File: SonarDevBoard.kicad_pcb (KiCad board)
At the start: 6 copper layers, 540 x 106.9 mm, 374 parts, among them J1001 TX_OUT_GAIN, J101 POWER, J102 DEBUG, J103 PORT1, J104 FPGA, J105 ETHERNET, J106 SYNC, J107 SONAR+, J108 SONAR+, J109 SONAR-, J110 SONAR-, J111 TRANSDUCER, J112 MOTOR, J1201 RFBT, J1202 RDAC, J401 RX_IN, J402 PREAMP, J403 BIAS_RES, J404 BIAS_RES, J405 GAIN_RES, J406 LPF_CAP, J407 VARAMP_OUT, J501 LABEL, J502 LABEL, J601 CAP, J901 OCTOSPI, Q101 DMP6023LSS-13, Q1201 SQJ974EP, Q1501 MMBT3904L, Q1502 MMBT3904L, Q1503 MMBT3904L, T101 B65655B0010X000, T701 HR641680E, U1001 SL9062D, U1002 LT1794, U1003 CSA230PASOT235, U101 LIS2DH12TR, U1101 TLV62569DBVR, U1201 LM5122MHX/NOPB, U1202 DAC53401DSGR, U1301 LM27313XMFX/NOPB, U1401 MG78L05T3, U1501 EPC23104ENGRT, U1502 EPC23104ENGRT, U1601 DRV8426RGER, U301 STM32H563AII3Q, U401 MD0100DK6-G, U402 OPA1612AIDR, U403 AD8338ACPZ-R7, U404 WS72552M-8/TR, U601 DAC53401DSGR, U602 DAC53401DSGR, U603 74LVC1G66GW,125, U701 DP83825IRMQR, U801 MIC28517T-E/PHA, U901 S27KL0642DPBHB023, X301 25MHz 8pF

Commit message: Finish VCC boost layout, realize that not enough power can be delivered to it
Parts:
- moved C1210 80.7 mm to (159.3, -76.1), turned to 90 degrees
- moved C1209 79.1 mm to (160.5, -76.1), turned to -90 degrees
- moved C1202 42.3 mm to (182.6, -84.5), turned to 180 degrees
- moved J1201 38.8 mm to (170.2, -89.0), turned to 90 degrees
- moved L1201 37.3 mm to (206.1, -75.2), turned to -90 degrees
- moved J1202 36.8 mm to (180.1, -89.0), turned to 90 degrees
- moved R1205 35.7 mm to (186.7, -81.2), turned to -90 degrees
- moved U1201 35.7 mm to (181.1, -79.0), turned to -90 degrees
- moved NT1201 34.0 mm to (151.4, -83.3)
- moved C1212 33.3 mm to (178.9, -72.0)
- moved C1208 33.3 mm to (167.9, -77.8)
- moved R1206 31.4 mm to (171.4, -86.7)
- moved C1211 29.9 mm to (176.1, -72.0)
- moved Q1201 25.9 mm to (183.1, -68.7)
- moved C1206 25.7 mm to (185.0, -76.5), turned to -90 degrees
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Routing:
- net /Power/VCC Boost/LO: track 0.00 -> 5.71 mm, vias 0 -> 2
- net /Power/VCC Boost/HO: track 0.00 -> 5.70 mm, vias 0 -> 2
- net /Power/VCC Boost/VIN_SENSED: track 0.00 -> 5.56 mm
- net GND: track 8.26 -> 13.8 mm, vias 25 -> 39
- net Net-(J1202-Pin_2): track 0.00 -> 4.74 mm
- net /VCC_EN: track 0.00 -> 4.66 mm
- net Net-(U1201-RES): track 0.00 -> 3.77 mm
- net /Power/VCC Boost/SOURCE: track 0.00 -> 3.27 mm
- net Net-(U1201-SLOPE): track 0.00 -> 2.66 mm
- net Net-(D1201-K): track 0.00 -> 2.59 mm
- net Net-(U1201-SS): track 0.00 -> 2.01 mm
- net Net-(U1201-COMP): track 0.00 -> 1.86 mm
- net /Power/VCC Boost/VCC: track 0.00 -> 1.75 mm
- net Net-(U1201-SYNCIN/RT): track 0.00 -> 1.37 mm
- net 3V3: track 2.68 -> 3.97 mm
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- added copper zone on F.Cu, net /Power/VCC Boost/PGND
- added copper zone on F.Cu, net /Power/VCC Boost/SOURCE
- added copper zone on F.Cu, net /Power/VCC Boost/VIN_SENSED
- added copper zone on F.Cu, net VCC
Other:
- board size 540 x 106.9 mm -> 110 x 60 mm

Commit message: Make a note that more output capacitance is required
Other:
- board size 110 x 60 mm -> 480.1 x 265.6 mm
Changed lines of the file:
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@@
+		(layer "Edge.Cuts")
+	)
+	(gr_rect
+		(start 38.7 -121.3)
+		(end 518.8 -14.65)
+		(stroke
+			(width 0.05)
+			(type default)
+		)
+		(fill no)
 		(layer "Edge.Cuts")
 	)

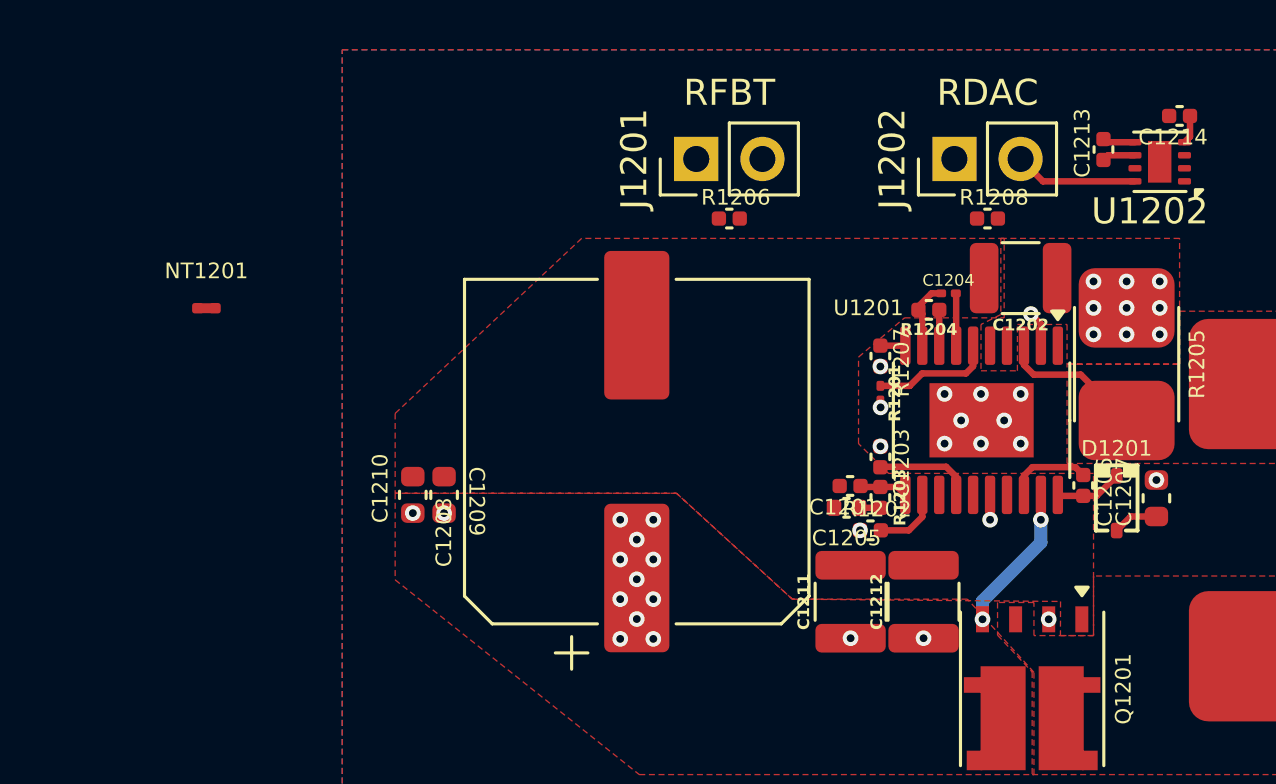
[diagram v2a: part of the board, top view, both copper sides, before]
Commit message: Finish VCC boost before adding more output capacitance
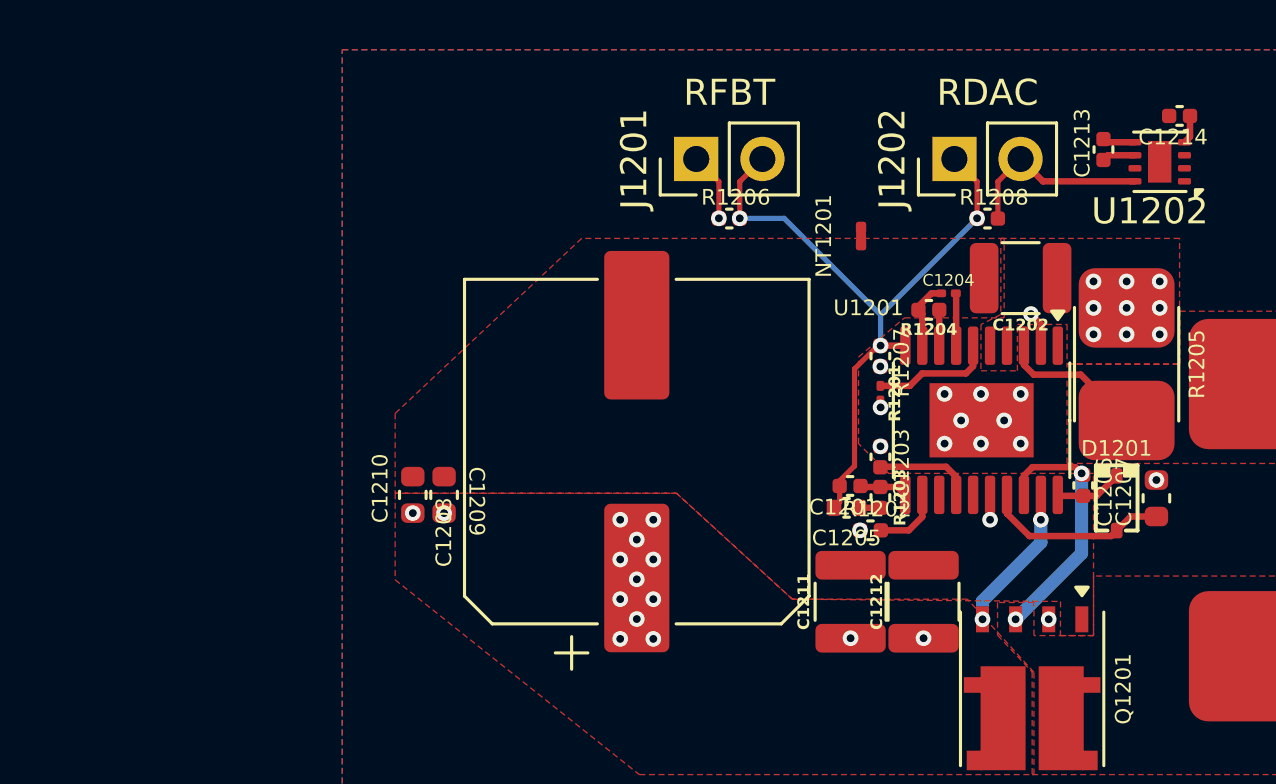
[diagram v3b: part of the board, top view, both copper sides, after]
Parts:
- moved NT1201 25.3 mm to (176.5, -86.1), turned to 90 degrees
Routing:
- net /Power/VCC Boost/FB: track 0.96 -> 26.6 mm, vias 0 -> 3
- net VCC: track 0.00 -> 15.3 mm, vias 15 -> 16
- net /Power/VCC Boost/SOURCE: track 3.27 -> 9.92 mm, vias 0 -> 2
- net /Power/VCC Boost/VCC: track 1.75 -> 7.12 mm
- net Net-(J1202-Pin_2): track 4.74 -> 7.39 mm

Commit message: Update power layout positions
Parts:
- added C1215: 220uF 100V, BR_Passives:C_Elec_12.5x12.5, F.Cu at (197.4, -207.2)
- added C1216: 220uF 100V, BR_Passives:C_Elec_12.5x12.5, F.Cu at (197.4, -192.6)
- added C1217: 220uF 100V, BR_Passives:C_Elec_12.5x12.5, F.Cu at (197.4, -178.1)
- added C1218: 220uF 100V, BR_Passives:C_Elec_12.5x12.5, F.Cu at (197.4, -163.5)
- moved C1101 214.5 mm to (493.4, -28.9)
- moved L1101 214.5 mm to (495.9, -33.9)
- moved R1101 214.5 mm to (498.2, -30.4)
- moved R1102 214.5 mm to (498.2, -29.0)
- moved C1102 214.5 mm to (497.4, -30.4)
- moved NT1101 214.5 mm to (495.4, -29.3)
- moved U1101 214.5 mm to (495.4, -29.6)
- moved D1301 104.8 mm to (492.5, -63.6)
- moved R1302 104.8 mm to (495.6, -63.8)
- moved U1301 104.8 mm to (494.4, -66.1)
- moved C1301 104.8 mm to (493.8, -68.5)
- moved C1302 104.8 mm to (494.1, -62.9)
- moved C1303 104.8 mm to (494.0, -63.8)
- moved L1301 104.8 mm to (491.3, -66.1)
- moved R1301 104.8 mm to (495.4, -68.5)
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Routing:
- net /Power/7V: vias 3 -> 4
- net RX_5V: vias 1 -> 2
